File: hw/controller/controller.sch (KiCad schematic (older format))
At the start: 57 parts, among them J1 ARM-SWD, P1 USB_OTG, P10 GPIO, P11 VDD_SEL, P12 UART0, P13 SPI, P14 I2C0, P15 I2C1, P16 I2C2, P17 I2C3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

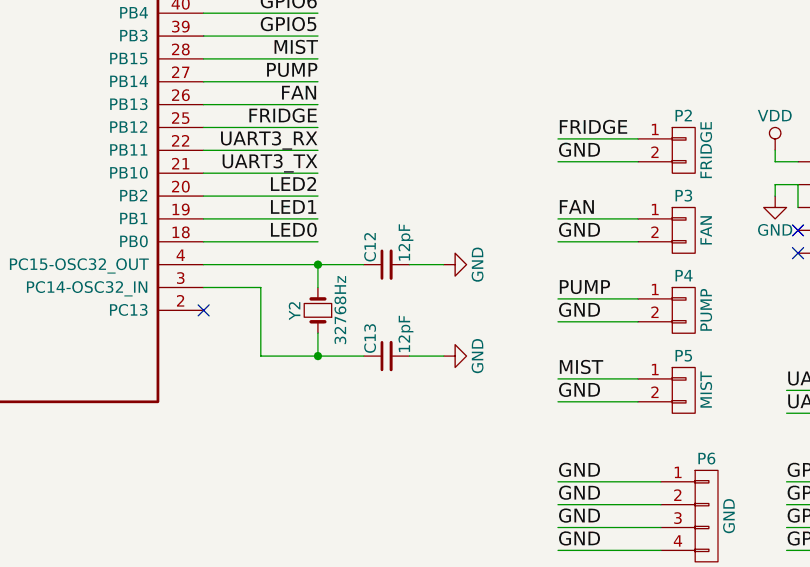
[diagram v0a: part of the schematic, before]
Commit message: RTC crystal update for schematic and BOM
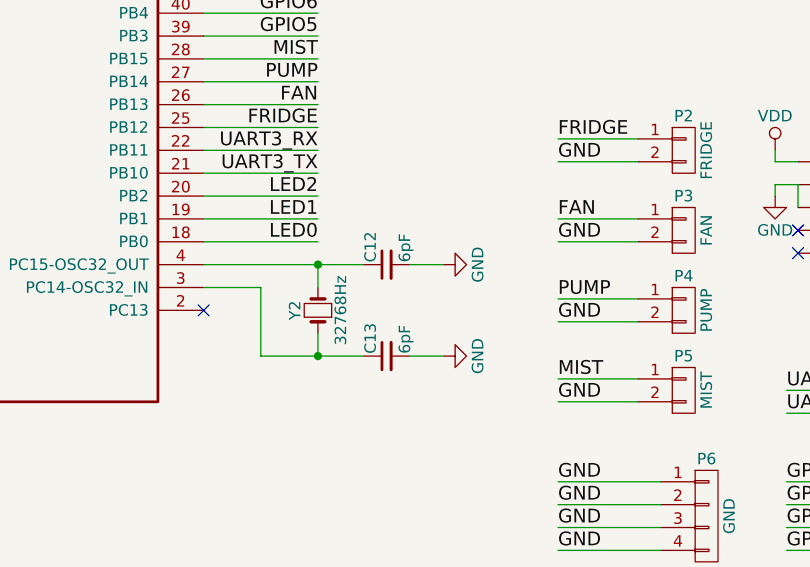
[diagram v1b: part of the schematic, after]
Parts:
- C12, C13: value 12pF -> 6pF; MPN CL10C120JB8NNNC -> CL10C060CB8NCNC
- Y2: MPN FC-135 32.7680KA-A0 -> ABS07-120-32.768KHZ-T
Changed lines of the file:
@@
 F 2 "footprints:FC-135" H 5000 4600 50  0001 C CNN
 F 3 "" H 5000 4600 50  0000 C CNN
-F 4 "FC-135 32.7680KA-A0" H 5000 4600 60  0001 C CNN "MPN"
+F 4 "ABS07-120-32.768KHZ-T" H 5000 4600 60  0001 C CNN "MPN"
 	1    5000 4600
 	0    -1   -1   0
@@
 P 5300 4800
 F 0 "C13" H 5310 4870 50  0000 L CNN
-F 1 "12pF" H 5310 4720 50  0000 L CNN
+F 1 "6pF" H 5310 4720 50  0000 L CNN
 F 2 "Capacitors_SMD:C_0603" H 5300 4800 50  0001 C CNN
 F 3 "" H 5300 4800 50  0000 C CNN
-F 4 "CL10C120JB8NNNC" H 5300 4800 60  0001 C CNN "MPN"
+F 4 "CL10C060CB8NCNC" H 5300 4800 60  0001 C CNN "MPN"
 	1    5300 4800
 	0    -1   -1   0
@@
 P 5300 4400
 F 0 "C12" H 5310 4470 50  0000 L CNN
-F 1 "12pF" H 5310 4320 50  0000 L CNN
+F 1 "6pF" H 5310 4320 50  0000 L CNN
 F 2 "Capacitors_SMD:C_0603" H 5300 4400 50  0001 C CNN
 F 3 "" H 5300 4400 50  0000 C CNN
-F 4 "CL10C120JB8NNNC" H 5300 4400 60  0001 C CNN "MPN"
+F 4 "CL10C060CB8NCNC" H 5300 4400 60  0001 C CNN "MPN"
 	1    5300 4400
 	0    -1   -1   0

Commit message: Updating ostur controller!
Removed unused headers
Added extra shielding for 32768Hz crystal
Made board smaller
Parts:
- removed P10, P9: GPIO, Pin_Headers:Pin_Header_Straight_1x04, symbol CONN_01X04
- removed P11: VDD_SEL, Pin_Headers:Pin_Header_Straight_1x03, symbol CONN_01X03
- removed P13: SPI, Pin_Headers:Pin_Header_Straight_1x04, symbol CONN_01X04
- removed P22: UART3, Pin_Headers:Pin_Header_Straight_1x02, symbol CONN_01X02
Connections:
- net labels removed: CS, GPIO0, GPIO1, GPIO2, GPIO3, GPIO4, GPIO5, GPIO6, GPIO7, MISO, MOSI, SCK, UART3_RX, UART3_TX, VDD_ALT
- wire segments 184 -> 150
- no-connect marks 11 -> 26
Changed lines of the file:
@@
 Sheet 1 1
 Title "Ostur Controller"
-Date "2017-01-11"
-Rev "1.1"
+Date "2017-02-04"
+Rev "1.2"
 Comp "alvarop.com"
 Comment1 ""
@@
 Text Label 1250 3900 0    60   ~ 0
 UART1_TX
-Text Label 1250 3700 0    60   ~ 0
-MOSI
-Text Label 1250 3600 0    60   ~ 0
-MISO
-Text Label 1250 3500 0    60   ~ 0
-SCK
-Text Label 1250 3400 0    60   ~ 0
-CS
-Text Label 1800 3000 2    60   ~ 0
-GPIO0
-Text Label 1800 3100 2    60   ~ 0
-GPIO1
-Text Label 1800 3200 2    60   ~ 0
-GPIO2
-Text Label 1800 3300 2    60   ~ 0
-GPIO3
 Text Label 6800 3050 0    60   ~ 0
 SDA
@@
 TCA_A1
 Text Label 6800 2850 0    60   ~ 0
-TCA_A2
-Text Label 5000 2800 2    60   ~ 0
 TCA_A2
 $Comp
@@
 	1    0    0    -1
 $EndComp
-Text Label 5000 4000 2    60   ~ 0
-UART3_TX
 Text Label 1250 4300 0    60   ~ 0
 SWDIO
-Text Label 5000 3900 2    60   ~ 0
-UART3_RX
-Text Label 5000 3800 2    60   ~ 0
+Text Label 1250 3600 2    60   ~ 0
 FRIDGE
-Text Label 5000 3700 2    60   ~ 0
+Text Label 1250 3500 2    60   ~ 0
 FAN
-Text Label 5000 3600 2    60   ~ 0
+Text Label 1250 3400 2    60   ~ 0
 PUMP
-Text Label 5000 3500 2    60   ~ 0
+Text Label 1250 3300 2    60   ~ 0
 MIST
-Text Label 5000 3400 2    60   ~ 0
-GPIO5
-Text Label 5000 3300 2    60   ~ 0
-GPIO6
-Text Label 5000 3200 2    60   ~ 0
-GPIO7
 Text Label 5000 4300 2    60   ~ 0
 LED0
@@
 Text Label 5000 4100 2    60   ~ 0
 LED2
-Text Label 1250 4500 0    60   ~ 0
-GPIO4
 $Comp
 L CONN_01X04 P14
@@
 $EndComp
 Text Label 8900 5350 0    60   ~ 0
-VDD_ALT
+VDD
 Text Label 8900 5450 0    60   ~ 0
 SCL2
@@
 $EndComp
 Text Label 8900 5900 0    60   ~ 0
-VDD_ALT
+VDD
 Text Label 8900 6000 0    60   ~ 0
 SCL3
@@
 Text Label 2750 7150 0    60   ~ 0
 LED2
-$Comp
-L CONN_01X04 P13
-U 1 1 5829C63F
-P 8600 6050
-F 0 "P13" H 8600 6300 50  0000 C CNN
-F 1 "SPI" V 8700 6050 50  0000 C CNN
-F 2 "Pin_Headers:Pin_Header_Straight_1x04" H 8600 6050 50  0001 C CNN
-F 3 "" H 8600 6050 50  0000 C CNN
-	1    8600 6050
-	1    0    0    -1
-$EndComp
 $Comp
 L CONN_01X06 P12
@@
 	0    -1   -1   0
 $EndComp
-Text Label 8000 5900 0    60   ~ 0
-MOSI
-Text Label 8000 6000 0    60   ~ 0
-MISO
-Text Label 8000 6100 0    60   ~ 0
-SCK
-Text Label 8000 6200 0    60   ~ 0
-CS
-$Comp
-L CONN_01X03 P11
-U 1 1 582A1820
-P 8600 4800
-F 0 "P11" H 8600 5000 50  0000 C CNN
-F 1 "VDD_SEL" V 8700 4800 50  0000 C CNN
-F 2 "Pin_Headers:Pin_Header_Straight_1x03" H 8600 4800 50  0001 C CNN
-F 3 "" H 8600 4800 50  0000 C CNN
-	1    8600 4800
-	1    0    0    -1
-$EndComp
-Text Label 8000 4800 0    60   ~ 0
-VDD_ALT
-Text Label 8000 4700 0    60   ~ 0
-VDD
-Text Label 8000 4900 0    60   ~ 0
-VDD_5
-$Comp
-L CONN_01X04 P10
-U 1 1 582A5612
-P 7700 6050
-F 0 "P10" H 7700 6300 50  0000 C CNN
-F 1 "GPIO" V 7800 6050 50  0000 C CNN
-F 2 "Pin_Headers:Pin_Header_Straight_1x04" H 7700 6050 50  0001 C CNN
-F 3 "" H 7700 6050 50  0000 C CNN
-	1    7700 6050
-	1    0    0    -1
-$EndComp
 $Comp
 L CONN_01X04 P6
@@
 Text Label 6050 5650 0    60   ~ 0
 GND
-Text Label 7050 5900 0    60   ~ 0
-GPIO4
-Text Label 7050 6000 0    60   ~ 0
-GPIO5
-Text Label 7050 6100 0    60   ~ 0
-GPIO6
-Text Label 7050 6200 0    60   ~ 0
-GPIO7
-$Comp
-L CONN_01X04 P9
-U 1 1 582A6318
-P 7700 5500
-F 0 "P9" H 7700 5750 50  0000 C CNN
-F 1 "GPIO" V 7800 5500 50  0000 C CNN
-F 2 "Pin_Headers:Pin_Header_Straight_1x04" H 7700 5500 50  0001 C CNN
-F 3 "" H 7700 5500 50  0000 C CNN
-	1    7700 5500
-	1    0    0    -1
-$EndComp
-Text Label 7050 5350 0    60   ~ 0
-GPIO0
-Text Label 7050 5450 0    60   ~ 0
-GPIO1
-Text Label 7050 5550 0    60   ~ 0
-GPIO2
-Text Label 7050 5650 0    60   ~ 0
-GPIO3
 $Comp
 L CONN_01X04 P7
@@
 NoConn ~ 5900 6950
 $Comp
-L CONN_01X02 P22
-U 1 1 582B6843
-P 7700 5000
-F 0 "P22" H 7700 5150 50  0000 C CNN
-F 1 "UART3" V 7800 5000 50  0000 C CNN
-F 2 "Pin_Headers:Pin_Header_Straight_1x02" H 7700 5000 50  0001 C CNN
-F 3 "" H 7700 5000 50  0000 C CNN
-	1    7700 5000
-	1    0    0    -1
-$EndComp
-Text Label 7050 5050 0    60   ~ 0
-UART3_TX
-Text Label 7050 4950 0    60   ~ 0
-UART3_RX
-$Comp
 L R R11
 U 1 1 582C3EF6
@@
 Connection ~ 3300 2000
 Wire Wire Line
-	3200 1800 3200 2000
+	3200 2000 3200 1800
 Wire Wire Line
 	3000 5200 3300 5200
@@
 	1250 3900 2000 3900
 Wire Wire Line
-	2000 3700 1250 3700
-Wire Wire Line
-	2000 3600 1250 3600
-Wire Wire Line
-	2000 3500 1250 3500
-Wire Wire Line
-	2000 3400 1250 3400
-Wire Wire Line
-	2000 3000 1800 3000
-Wire Wire Line
-	2000 3100 1800 3100
-Wire Wire Line
-	2000 3200 1800 3200
-Wire Wire Line
-	2000 3300 1800 3300
-Wire Wire Line
-	4500 3800 5000 3800
-Wire Wire Line
-	4500 3700 5000 3700
-Wire Wire Line
-	4500 3600 5000 3600
-Wire Wire Line
-	4500 3500 5000 3500
-Wire Wire Line
-	4500 4000 5000 4000
-Wire Wire Line
-	4500 3900 5000 3900
-Wire Wire Line
 	7100 3050 6800 3050
 Wire Wire Line
@@
 	6500 2750 7100 2750
 Wire Wire Line
-	7100 2850 6800 2850
-Wire Wire Line
-	4500 2800 5000 2800
-Wire Wire Line
-	6700 2650 6700 2550
+	6700 2850 7100 2850
+Wire Wire Line
+	6700 2550 6700 2850
 Connection ~ 6700 2550
 Wire Wire Line
@@
 Connection ~ 2600 1350
 Wire Wire Line
-	4500 3400 5000 3400
-Wire Wire Line
 	2000 4300 1250 4300
 Wire Wire Line
-	4500 3300 5000 3300
-Wire Wire Line
-	4500 3200 5000 3200
-Wire Wire Line
 	4500 4300 5000 4300
 Wire Wire Line
@@
 Wire Wire Line
 	4500 4100 5000 4100
-Wire Wire Line
-	2000 4500 1250 4500
 Wire Wire Line
 	9200 4250 8900 4250
@@
 	4250 6850 4250 6900
 Wire Wire Line
-	8400 5900 8000 5900
-Wire Wire Line
-	8400 6000 8000 6000
-Wire Wire Line
-	8400 6100 8000 6100
-Wire Wire Line
-	8400 6200 8000 6200
-Wire Wire Line
 	8400 5150 8000 5150
 Wire Wire Line
@@
 	4750 4500 4750 4800
 Wire Wire Line
-	8400 4800 8000 4800
-Wire Wire Line
-	8400 4700 8000 4700
-Wire Wire Line
-	8400 4900 8000 4900
-Wire Wire Line
 	6500 5350 6050 5350
 Wire Wire Line
@@
 Wire Wire Line
 	6500 5650 6050 5650
-Wire Wire Line
-	7500 5900 7050 5900
-Wire Wire Line
-	7500 6000 7050 6000
-Wire Wire Line
-	7500 6100 7050 6100
-Wire Wire Line
-	7500 6200 7050 6200
-Wire Wire Line
-	7500 5350 7050 5350
-Wire Wire Line
-	7500 5450 7050 5450
-Wire Wire Line
-	7500 5550 7050 5550
-Wire Wire Line
-	7500 5650 7050 5650
 Wire Wire Line
 	6500 5900 6050 5900
@@
 Connection ~ 3550 1100
 Wire Wire Line
-	7500 4950 7050 4950
-Wire Wire Line
-	7500 5050 7050 5050
-Wire Wire Line
 	10150 1200 10400 1200
 Wire Wire Line
 	10150 1350 10400 1350
 Wire Wire Line
-	9850 850  9850 1700
+	9850 850  9850 2500
 Wire Wire Line
 	10150 850  10400 850
@@
 Wire Wire Line
 	10150 1700 10400 1700
-Wire Wire Line
-	9850 2000 9850 2500
 Wire Wire Line
 	10150 2000 10400 2000
@@
 Wire Wire Line
 	9650 1550 9650 1450
-Wire Wire Line
-	9450 2150 9850 2150
-Text Label 9450 2150 0    60   ~ 0
-VDD_ALT
 $Comp
 L VDD #PWR022
@@
 	0    1    1    0
 $EndComp
+NoConn ~ 2000 3000
+NoConn ~ 2000 3700
+NoConn ~ 2000 4500
+NoConn ~ 4500 3400
+NoConn ~ 4500 3300
+NoConn ~ 4500 3200
+NoConn ~ 4500 3900
+NoConn ~ 4500 4000
+Connection ~ 9850 2000
+Connection ~ 6700 2650
+NoConn ~ 4500 2800
+NoConn ~ 2000 3200
+NoConn ~ 2000 3100
+Wire Wire Line
+	2000 3600 1250 3600
+Wire Wire Line
+	2000 3500 1250 3500
+Wire Wire Line
+	2000 3400 1250 3400
+Wire Wire Line
+	2000 3300 1250 3300
+NoConn ~ 4500 3500
+NoConn ~ 4500 3600
+NoConn ~ 4500 3700
+NoConn ~ 4500 3800
 $EndSCHEMATC

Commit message: something something kicad update....
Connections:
- wire segments 150 -> 151
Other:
- moved on the sheet: P1
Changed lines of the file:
@@
 EESchema Schematic File Version 2
+LIBS:controller-rescue
 LIBS:power
 LIBS:device
@@
 L USB_OTG P1
 U 1 1 582A896C
-P 6200 6850
-F 0 "P1" H 6525 6725 50  0000 C CNN
-F 1 "USB_OTG" H 6200 7050 50  0000 C CNN
-F 2 "footprints:USB_MICRO_B" V 6150 6750 50  0001 C CNN
-F 3 "" V 6150 6750 50  0000 C CNN
-F 4 "10118192-0001LF" H 6200 6850 60  0001 C CNN "MPN"
-	1    6200 6850
-	0    1    1    0
+P 6500 6850
+F 0 "P1" H 6825 6725 50  0000 C CNN
+F 1 "USB_OTG" H 6500 7050 50  0000 C CNN
+F 2 "footprints:USB_MICRO_B" V 6450 6750 50  0001 C CNN
+F 3 "" V 6450 6750 50  0000 C CNN
+F 4 "10118192-0001LF" H 6500 6850 60  0001 C CNN "MPN"
+	1    6500 6850
+	-1   0    0    1
 $EndComp
 $Comp
 L GND #PWR014
-U 1 1 582A8FAE
-P 5750 7150
-F 0 "#PWR014" H 5750 6900 50  0001 C CNN
-F 1 "GND" H 5750 7000 50  0000 C CNN
-F 2 "" H 5750 7150 50  0000 C CNN
-F 3 "" H 5750 7150 50  0000 C CNN
-	1    5750 7150
-	1    0    0    -1
-$EndComp
-$Comp
-L GND #PWR015
 U 1 1 582A906E
-P 6300 7250
-F 0 "#PWR015" H 6300 7000 50  0001 C CNN
-F 1 "GND" H 6300 7100 50  0000 C CNN
-F 2 "" H 6300 7250 50  0000 C CNN
-F 3 "" H 6300 7250 50  0000 C CNN
-	1    6300 7250
-	1    0    0    -1
-$EndComp
-$Comp
-L +5V #PWR016
+P 6700 6400
+F 0 "#PWR014" H 6700 6150 50  0001 C CNN
+F 1 "GND" H 6700 6250 50  0000 C CNN
+F 2 "" H 6700 6400 50  0000 C CNN
+F 3 "" H 6700 6400 50  0000 C CNN
+	1    6700 6400
+	0    -1   -1   0
+$EndComp
+$Comp
+L +5V #PWR015
 U 1 1 582A97A5
-P 5350 6550
-F 0 "#PWR016" H 5350 6400 50  0001 C CNN
-F 1 "+5V" H 5350 6690 50  0000 C CNN
-F 2 "" H 5350 6550 50  0000 C CNN
-F 3 "" H 5350 6550 50  0000 C CNN
-	1    5350 6550
-	1    0    0    -1
-$EndComp
-Text Label 5400 6650 0    60   ~ 0
+P 5650 7150
+F 0 "#PWR015" H 5650 7000 50  0001 C CNN
+F 1 "+5V" H 5650 7290 50  0000 C CNN
+F 2 "" H 5650 7150 50  0000 C CNN
+F 3 "" H 5650 7150 50  0000 C CNN
+	1    5650 7150
+	-1   0    0    1
+$EndComp
+Text Label 5700 7050 0    60   ~ 0
 VDD_5
 $Comp
@@
 $EndComp
 $Comp
-L GND #PWR017
+L GND #PWR016
 U 1 1 582AE5E7
 P 4200 1400
-F 0 "#PWR017" H 4200 1150 50  0001 C CNN
+F 0 "#PWR016" H 4200 1150 50  0001 C CNN
 F 1 "GND" H 4200 1250 50  0000 C CNN
 F 2 "" H 4200 1400 50  0000 C CNN
@@
 $EndComp
 $Comp
-L VDD #PWR018
+L VDD #PWR017
 U 1 1 582AE68B
 P 4850 950
-F 0 "#PWR018" H 4850 800 50  0001 C CNN
+F 0 "#PWR017" H 4850 800 50  0001 C CNN
 F 1 "VDD" H 4850 1100 50  0000 C CNN
 F 2 "" H 4850 950 50  0000 C CNN
@@
 $EndComp
 $Comp
-L +5V #PWR019
+L +5V #PWR018
 U 1 1 582AEA2C
 P 3550 950
-F 0 "#PWR019" H 3550 800 50  0001 C CNN
+F 0 "#PWR018" H 3550 800 50  0001 C CNN
 F 1 "+5V" H 3550 1090 50  0000 C CNN
 F 2 "" H 3550 950 50  0000 C CNN
@@
 $EndComp
 $Comp
-L VDD #PWR020
+L VDD #PWR019
 U 1 1 582AFB4F
 P 7000 3900
-F 0 "#PWR020" H 7000 3750 50  0001 C CNN
+F 0 "#PWR019" H 7000 3750 50  0001 C CNN
 F 1 "VDD" H 7000 4050 50  0000 C CNN
 F 2 "" H 7000 3900 50  0000 C CNN
@@
 $EndComp
 $Comp
-L GND #PWR021
+L GND #PWR020
 U 1 1 582AFC2A
 P 7000 4100
-F 0 "#PWR021" H 7000 3850 50  0001 C CNN
+F 0 "#PWR020" H 7000 3850 50  0001 C CNN
 F 1 "GND" H 7000 3950 50  0000 C CNN
 F 2 "" H 7000 4100 50  0000 C CNN
@@
 	1    0    0    -1
 $EndComp
-NoConn ~ 5900 6950
+NoConn ~ 6200 6650
 $Comp
 L R R11
@@
 	9200 6100 8900 6100
 Wire Wire Line
-	3300 7150 3400 7150
-Wire Wire Line
-	3300 6850 3400 6850
-Wire Wire Line
-	3300 6550 3400 6550
+	3300 7150 3450 7150
+Wire Wire Line
+	3300 6850 3450 6850
+Wire Wire Line
+	3300 6550 3450 6550
 Wire Wire Line
 	3000 6550 2750 6550
@@
 	3000 7150 2750 7150
 Wire Wire Line
-	3800 6550 4050 6550
-Wire Wire Line
-	3800 6850 4250 6850
-Wire Wire Line
-	4050 7150 3800 7150
-Wire Wire Line
-	4050 6550 4050 7150
+	3750 6550 4050 6550
+Wire Wire Line
+	3750 6850 4250 6850
+Wire Wire Line
+	3750 7150 4050 7150
+Wire Wire Line
+	4050 7150 4050 6550
 Connection ~ 4050 6850
 Wire Wire Line
@@
 	6400 5000 6050 5000
 Wire Wire Line
-	5900 6650 5350 6650
-Wire Wire Line
-	5350 6650 5350 6550
-Wire Wire Line
-	5900 7050 5750 7050
-Wire Wire Line
-	5750 7050 5750 7150
-Wire Wire Line
-	5900 6750 5600 6750
-Wire Wire Line
-	5900 6850 5750 6850
+	6200 7050 5650 7050
+Wire Wire Line
+	5600 6750 6200 6750
+Wire Wire Line
+	5750 6850 6200 6850
 Wire Wire Line
 	5750 6850 5750 6950
@@
 	9650 1550 9650 1450
 $Comp
-L VDD #PWR022
+L VDD #PWR021
 U 1 1 582C95F9
 P 9650 1450
-F 0 "#PWR022" H 9650 1300 50  0001 C CNN
+F 0 "#PWR021" H 9650 1300 50  0001 C CNN
 F 1 "VDD" H 9650 1600 50  0000 C CNN
 F 2 "" H 9650 1450 50  0000 C CNN
@@
 $EndComp
 $Comp
-L PWR_FLAG #FLG023
+L PWR_FLAG #FLG022
 U 1 1 582CCD04
 P 3000 5250
-F 0 "#FLG023" H 3000 5345 50  0001 C CNN
+F 0 "#FLG022" H 3000 5345 50  0001 C CNN
 F 1 "PWR_FLAG" H 3000 5430 50  0000 C CNN
 F 2 "" H 3000 5250 50  0000 C CNN
@@
 Connection ~ 3200 1850
 $Comp
-L PWR_FLAG #FLG024
+L PWR_FLAG #FLG023
 U 1 1 587743C2
 P 3550 2000
-F 0 "#FLG024" H 3550 2095 50  0001 C CNN
+F 0 "#FLG023" H 3550 2095 50  0001 C CNN
 F 1 "PWR_FLAG" H 3550 2180 50  0000 C CNN
 F 2 "" H 3550 2000 50  0000 C CNN
@@
 NoConn ~ 4500 3700
 NoConn ~ 4500 3800
+Wire Wire Line
+	6600 6450 6600 6400
+Wire Wire Line
+	6500 6400 6700 6400
+Wire Wire Line
+	6500 6450 6500 6400
+Connection ~ 6600 6400
+Wire Wire Line
+	5650 7050 5650 7150
+$Comp
+L PWR_FLAG #FLG?
+U 1 1 58C44F8F
+P 5900 7050
+F 0 "#FLG?" H 5900 7125 50  0001 C CNN
+F 1 "PWR_FLAG" H 5900 7200 50  0000 C CNN
+F 2 "" H 5900 7050 50  0001 C CNN
+F 3 "" H 5900 7050 50  0001 C CNN
+	1    5900 7050
+	-1   0    0    1
+$EndComp
+Connection ~ 5900 7050
 $EndSCHEMATC
